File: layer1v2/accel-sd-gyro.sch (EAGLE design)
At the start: 7 parts, among them U1 MMA8452Q

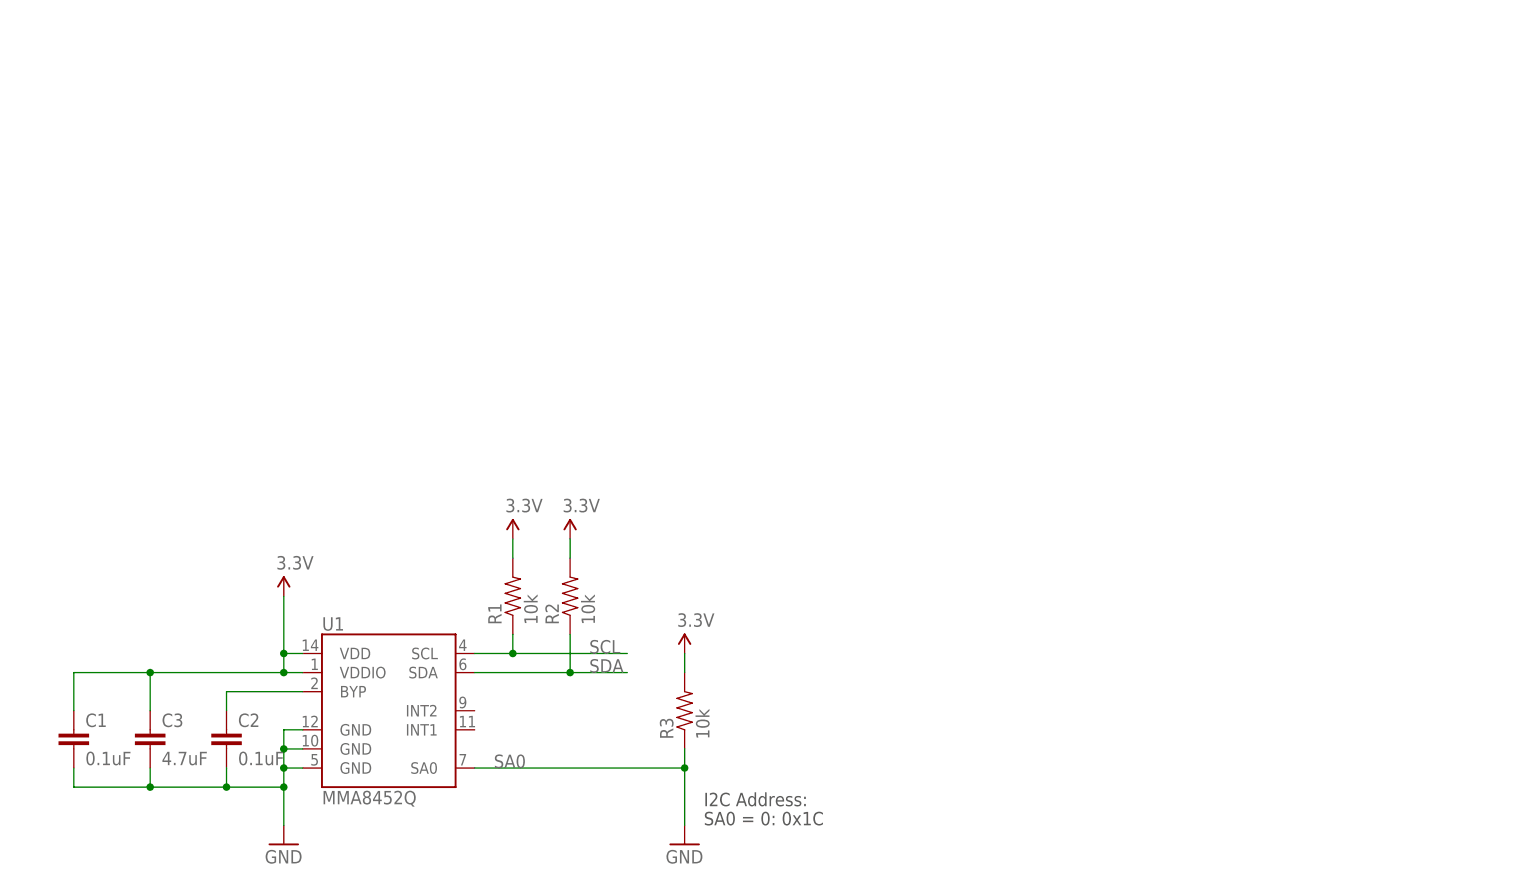
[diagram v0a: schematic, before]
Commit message: added gyro
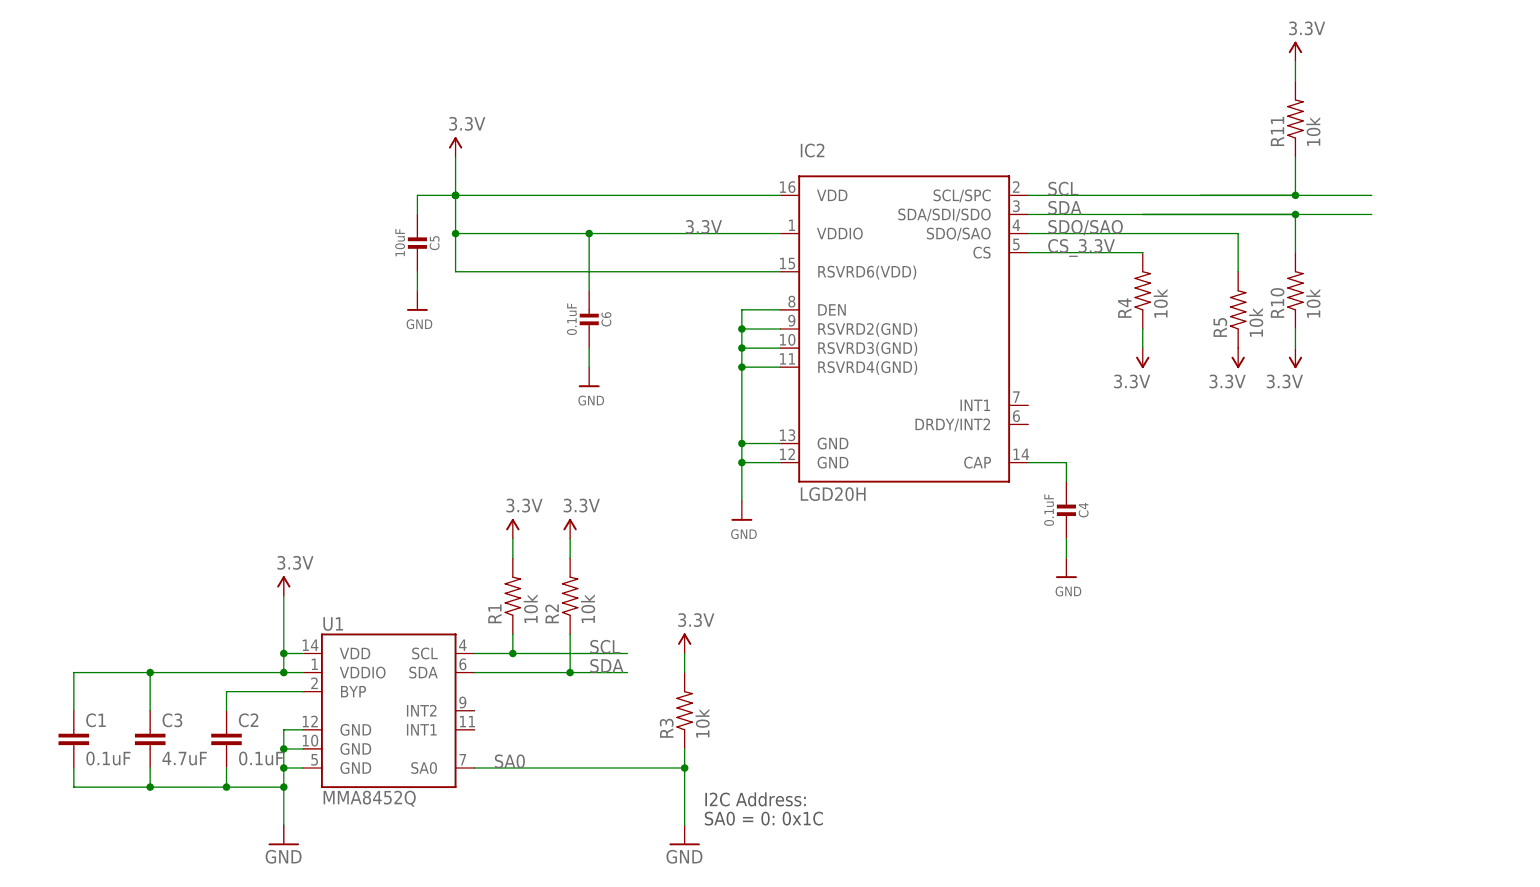
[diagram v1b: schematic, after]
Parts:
- added C4, C6: 0.1uF, microbuilder:CAP_CERAMIC0805-NOOUTLINE
- added C5: 10uF, microbuilder:CAP_CERAMIC0805-NOOUTLINE
- added IC2: LGD20H, microbuilder:GYRO_L3GD20H
- added R10, R11, R4, R5: 10k, SparkFun:RESISTOR0402-RES
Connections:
- new net CS_3.3V: IC2.CS, R4.2
- new net N$3: C4.2, IC2.CAP
- new net SDO/SAO: IC2.SDO/SAO, R5.2
- net 3.3V: now also C5.2, C6.2, IC2.RSVRD6(VDD), IC2.VDD, IC2.VDDIO, R10.1, R11.2, R4.1, R5.1
- net GND: now also C4.1, C5.1, C6.1, IC2.DEN, IC2.GND@1, IC2.GND@2, IC2.RSVRD2(GND), IC2.RSVRD3(GND), IC2.RSVRD4(GND)
- net SCL: now also IC2.SCL/SPC, R11.1
- net SDA: now also IC2.SDA/SDI/SDO, R10.2

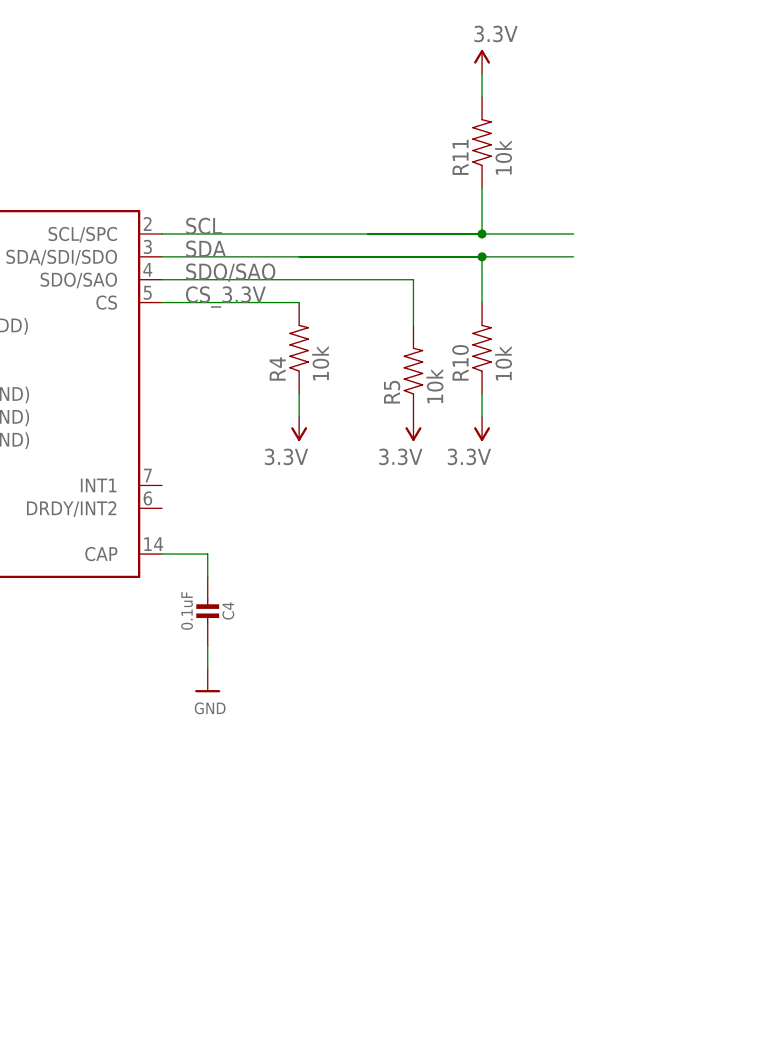
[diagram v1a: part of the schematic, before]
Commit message: added sd
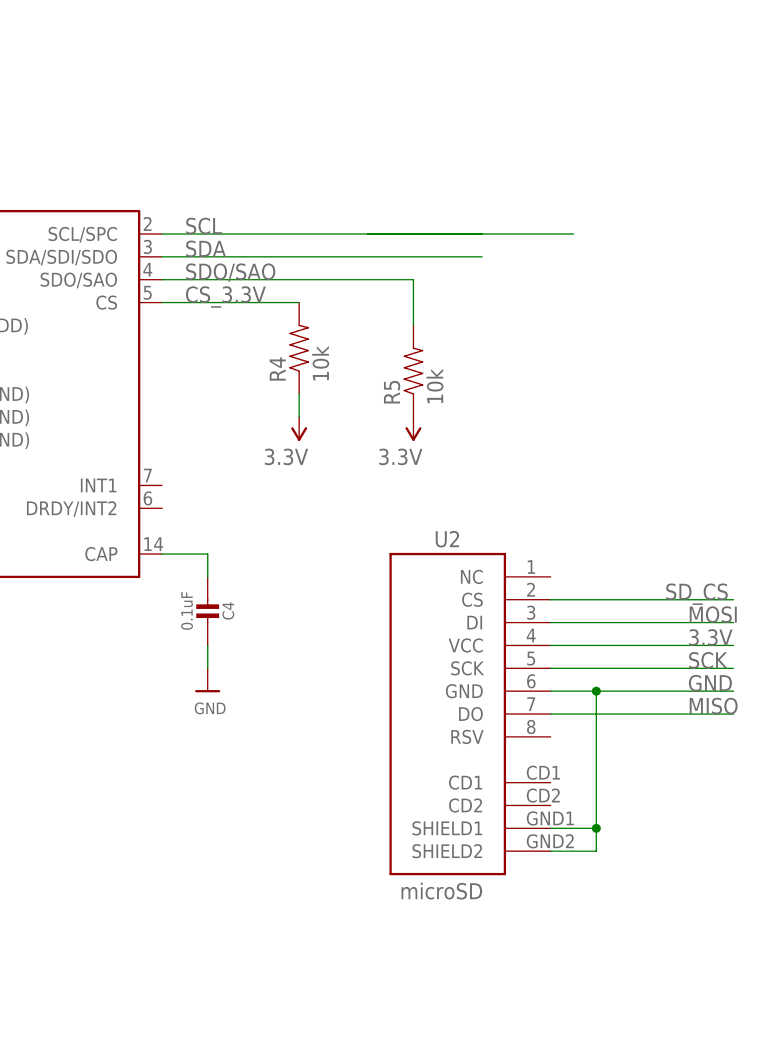
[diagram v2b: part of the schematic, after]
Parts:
- removed R10, R11: 10k, SparkFun:RESISTOR0402-RES
- added U2: microSD, SparkFun:USD-SOCKETSMD
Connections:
- new net MISO: U2.DO
- new net MOSI: U2.DI
- new net SCK: U2.SCK
- new net SD_CS: U2.CS
- net 3.3V: now also U2.VCC; no longer R10.1, R11.2
- net GND: now also U2.GND, U2.SHIELD1, U2.SHIELD2
- net SCL: no longer R11.1
- net SDA: no longer R10.2
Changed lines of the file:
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@@
 <setting verticaltext="up"/>
 </settings>
-<grid distance="0.1" unitdist="inch" unit="inch" style="lines" multiple="1" display="yes" altdistance="0.01" altunitdist="inch" altunit="inch"/>
+<grid distance="0.1" unitdist="inch" unit="inch" style="lines" multiple="1" display="no" altdistance="0.01" altunitdist="inch" altunit="inch"/>
 <layers>
 <layer number="1" name="Top" color="4" fill="1" visible="no" active="no"/>
@@
 <part name="R4" library="SparkFun" deviceset="RESISTOR" device="0402-RES" value="10k"/>
 <part name="R5" library="SparkFun" deviceset="RESISTOR" device="0402-RES" value="10k"/>
-<part name="R10" library="SparkFun" deviceset="RESISTOR" device="0402-RES" value="10k"/>
-<part name="R11" library="SparkFun" deviceset="RESISTOR" device="0402-RES" value="10k"/>
 <part name="P+5" library="SparkFun" deviceset="3.3V" device=""/>
-<part name="P+6" library="SparkFun" deviceset="3.3V" device=""/>
 <part name="P+7" library="SparkFun" deviceset="3.3V" device=""/>
 <part name="P+8" library="SparkFun" deviceset="3.3V" device=""/>
-<part name="P+9" library="SparkFun" deviceset="3.3V" device=""/>
+<part name="U2" library="SparkFun" deviceset="USD-SOCKET" device="SMD" value="microSD"/>
 </parts>
 <sheets>
@@
 <instance part="R4" gate="G$1" x="157.48" y="121.92" rot="R90"/>
 <instance part="R5" gate="G$1" x="170.18" y="119.38" rot="R90"/>
-<instance part="R10" gate="G$1" x="177.8" y="121.92" rot="R90"/>
-<instance part="R11" gate="G$1" x="177.8" y="144.78" rot="R90"/>
 <instance part="P+5" gate="G$1" x="66.04" y="139.7"/>
-<instance part="P+6" gate="G$1" x="177.8" y="152.4"/>
 <instance part="P+7" gate="G$1" x="157.48" y="114.3" rot="R180"/>
 <instance part="P+8" gate="G$1" x="170.18" y="114.3" rot="R180"/>
-<instance part="P+9" gate="G$1" x="177.8" y="114.3" rot="R180"/>
+<instance part="U2" gate="G$1" x="177.8" y="83.82" smashed="yes" rot="MR0">
+<attribute name="NAME" x="172.466" y="99.822" size="1.778" layer="95"/>
+<attribute name="VALUE" x="168.656" y="60.706" size="1.778" layer="96"/>
+</instance>
 </instances>
 <busses>
@@
 </segment>
 <segment>
-<wire x1="177.8" y1="152.4" x2="177.8" y2="149.86" width="0.1524" layer="91"/>
-<pinref part="R11" gate="G$1" pin="2"/>
-<pinref part="P+6" gate="G$1" pin="3.3V"/>
-</segment>
-<segment>
-<wire x1="177.8" y1="114.3" x2="177.8" y2="116.84" width="0.1524" layer="91"/>
-<pinref part="R10" gate="G$1" pin="1"/>
-<pinref part="P+9" gate="G$1" pin="3.3V"/>
-</segment>
-<segment>
 <pinref part="R5" gate="G$1" pin="1"/>
 <pinref part="P+8" gate="G$1" pin="3.3V"/>
@@
 <pinref part="R4" gate="G$1" pin="1"/>
 <pinref part="P+7" gate="G$1" pin="3.3V"/>
+</segment>
+<segment>
+<wire x1="185.42" y1="88.9" x2="205.74" y2="88.9" width="0.1524" layer="91"/>
+<pinref part="U2" gate="G$1" pin="VCC"/>
+<label x="200.66" y="88.9" size="1.778" layer="95"/>
 </segment>
 </net>
@@
 <pinref part="U$7" gate="G$1" pin="GND"/>
 </segment>
+<segment>
+<wire x1="185.42" y1="83.82" x2="190.5" y2="83.82" width="0.1524" layer="91"/>
+<wire x1="190.5" y1="83.82" x2="205.74" y2="83.82" width="0.1524" layer="91"/>
+<wire x1="185.42" y1="66.04" x2="190.5" y2="66.04" width="0.1524" layer="91"/>
+<wire x1="190.5" y1="66.04" x2="190.5" y2="68.58" width="0.1524" layer="91"/>
+<wire x1="190.5" y1="68.58" x2="190.5" y2="83.82" width="0.1524" layer="91"/>
+<wire x1="185.42" y1="68.58" x2="190.5" y2="68.58" width="0.1524" layer="91"/>
+<junction x="190.5" y="83.82"/>
+<junction x="190.5" y="68.58"/>
+<pinref part="U2" gate="G$1" pin="GND"/>
+<pinref part="U2" gate="G$1" pin="SHIELD1"/>
+<pinref part="U2" gate="G$1" pin="SHIELD2"/>
+<label x="200.66" y="83.82" size="1.778" layer="95"/>
+</segment>
 </net>
 <net name="SCL" class="0">
@@
 </segment>
 <segment>
-<wire x1="177.8" y1="134.62" x2="165.1" y2="134.62" width="0.1524" layer="91"/>
-<wire x1="177.8" y1="134.62" x2="177.8" y2="139.7" width="0.1524" layer="91"/>
-<wire x1="142.24" y1="134.62" x2="177.8" y2="134.62" width="0.1524" layer="91"/>
-<junction x="177.8" y="134.62"/>
+<wire x1="142.24" y1="134.62" x2="187.96" y2="134.62" width="0.1524" layer="91"/>
 <label x="144.78" y="134.62" size="1.778" layer="95"/>
 <pinref part="IC2" gate="G$1" pin="SCL/SPC"/>
-<wire x1="177.8" y1="134.62" x2="187.96" y2="134.62" width="0.1524" layer="91"/>
-<pinref part="R11" gate="G$1" pin="1"/>
 </segment>
 </net>
@@
 </segment>
 <segment>
-<wire x1="177.8" y1="127" x2="177.8" y2="132.08" width="0.1524" layer="91"/>
-<wire x1="157.48" y1="132.08" x2="177.8" y2="132.08" width="0.1524" layer="91"/>
 <wire x1="142.24" y1="132.08" x2="177.8" y2="132.08" width="0.1524" layer="91"/>
-<junction x="177.8" y="132.08"/>
 <label x="144.78" y="132.08" size="1.778" layer="95"/>
 <pinref part="IC2" gate="G$1" pin="SDA/SDI/SDO"/>
-<wire x1="177.8" y1="132.08" x2="187.96" y2="132.08" width="0.1524" layer="91"/>
-<pinref part="R10" gate="G$1" pin="2"/>
 </segment>
 </net>
@@
 <net name="+3V1" class="0">
 </net>
+<net name="N$1" class="0">
+<segment>
+<wire x1="177.8" y1="134.62" x2="165.1" y2="134.62" width="0.1524" layer="91"/>
+</segment>
+</net>
+<net name="SD_CS" class="0">
+<segment>
+<wire x1="185.42" y1="93.98" x2="205.74" y2="93.98" width="0.1524" layer="91"/>
+<pinref part="U2" gate="G$1" pin="CS"/>
+<label x="198.12" y="93.98" size="1.778" layer="95"/>
+</segment>
+</net>
+<net name="MOSI" class="0">
+<segment>
+<wire x1="185.42" y1="91.44" x2="205.74" y2="91.44" width="0.1524" layer="91"/>
+<pinref part="U2" gate="G$1" pin="DI"/>
+<label x="200.66" y="91.44" size="1.778" layer="95"/>
+</segment>
+</net>
+<net name="SCK" class="0">
+<segment>
+<wire x1="185.42" y1="86.36" x2="205.74" y2="86.36" width="0.1524" layer="91"/>
+<pinref part="U2" gate="G$1" pin="SCK"/>
+<label x="200.66" y="86.36" size="1.778" layer="95"/>
+</segment>
+</net>
+<net name="MISO" class="0">
+<segment>
+<wire x1="185.42" y1="81.28" x2="205.74" y2="81.28" width="0.1524" layer="91"/>
+<pinref part="U2" gate="G$1" pin="DO"/>
+<label x="200.66" y="81.28" size="1.778" layer="95"/>
+</segment>
+</net>
 </nets>
